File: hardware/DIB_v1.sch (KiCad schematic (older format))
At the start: 2 parts, among them J1 20-pin power socket, J2 Conn_02x14_Odd_Even

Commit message: Adding Bias_PS from dcm220
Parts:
- added C? (x4): 100n, EEZ DIB DCM220 r2B7:C0603, symbol EEZ_DIB_DCM220_r2B7-eagle-import:C-EUC0603
- added IC?: Si8662AB-B-IS1, EEZ DIB DCM220 r2B7:SOIC-16, symbol EEZ_DIB_DCM220_r2B7-eagle-import:SI8662NSOIC-16
- added IC?: Si8641AB-B-IS1, EEZ DIB DCM220 r2B7:SOIC-16, symbol EEZ_DIB_DCM220_r2B7-eagle-import:SI8641NSOIC-16
- added RN? (x4): DR1206-33R-4/8, EEZ DIB DCM220 r2B7:CAY16, symbol EEZ_DIB_DCM220_r2B7-eagle-import:R_ARRAY4
- added TX_PU?: 10K, EEZ DIB DCM220 r2B7:R0805, symbol EEZ_DIB_DCM220_r2B7-eagle-import:R-EU_R0805
- added X? (x24): 77317-104-28LF, EEZ DIB DCM220 r2B7:77317-104-28LF, symbol EEZ_DIB_DCM220_r2B7-eagle-import:77317-104-28LF
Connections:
- net labels added: +3V3, +VAUX, BOOT0, DIB_A0, DIB_A1, DIB_A2, DIB_BOOT0, DIB_CSA, DIB_CSB, DIB_IRQ, DIB_MISO, DIB_MOSI, DIB_NFAULT, DIB_NRESET, DIB_SCL, DIB_SCLK, DIB_SDA, DIB_SYNC, DIB_UART_RX, DIB_UART_TX, GND, GNDIO, IRQ, MISO, MOSI, NSS, OE_SYNC, SCLK, UART_RX, UART_TX, V+, ~RESET
- wire segments 20 -> 111
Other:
- note added: "+12V 21"
- note added: "+3V3 1"
- note added: "+5V 23"
- note added: "10 DIB_IRQ"
- note added: "12 DIB_CSB"
- note added: "14 DIB_MISO"
- note added: "16 Gnd"
- note added: "18 DIB_A2"
- note added: "2 +Vaux"
- note added: "20 Gnd"
- note added: "22 +12V"
- note added: "24 +5V"
- note added: "26 BOOT"
- note added: "28 UART_TX"
- note added: "28-pin module socket"
- note added: "4 NRESET"
- note added: "6 OE_SYNC"
- note added: "8 DIB_SDA"
- note added: "Bus isolator"
- note added: "DIB v1.0 connector"
- note added: "DIB_A0 17"
- note added: "DIB_A1 19"
- note added: "DIB_CSA 9"
- note added: "DIB_MOSI 15"
- note added: "DIB_SCL 5"
- note added: "DIB_SCLK 13"
- note added: "Gnd 11"
- note added: "Gnd 25"
- note added: "Gnd 7"
- note added: "Max. transfer speed is 1MBit/s"
- note added: "NFAULT 3"
- note added: "UART_RX 27"

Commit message: Adding ULX3S connections
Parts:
- removed C? (x4): 100n, EEZ DIB DCM220 r2B7:C0603, symbol EEZ_DIB_DCM220_r2B7-eagle-import:C-EUC0603
- removed IC?: Si8662AB-B-IS1, EEZ DIB DCM220 r2B7:SOIC-16, symbol EEZ_DIB_DCM220_r2B7-eagle-import:SI8662NSOIC-16
- removed IC?: Si8641AB-B-IS1, EEZ DIB DCM220 r2B7:SOIC-16, symbol EEZ_DIB_DCM220_r2B7-eagle-import:SI8641NSOIC-16
- removed J2: Conn_02x14_Odd_Even, Connector_PinHeader_2.54mm:PinHeader_2x14_P2.54mm_Horizontal, symbol Connector_Generic:Conn_02x14_Odd_Even
- removed RN? (x4): DR1206-33R-4/8, EEZ DIB DCM220 r2B7:CAY16, symbol EEZ_DIB_DCM220_r2B7-eagle-import:R_ARRAY4
- removed TX_PU?: 10K, EEZ DIB DCM220 r2B7:R0805, symbol EEZ_DIB_DCM220_r2B7-eagle-import:R-EU_R0805
- removed X? (x24): 77317-104-28LF, EEZ DIB DCM220 r2B7:77317-104-28LF, symbol EEZ_DIB_DCM220_r2B7-eagle-import:77317-104-28LF
- added J3: 28-pin module socket, Connector_PinHeader_2.54mm:PinHeader_2x14_P2.54mm_Horizontal, symbol Connector_Generic:Conn_02x14_Odd_Even
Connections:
- net labels added: +12V, +5V, A0, A1, A2, BOOT, CSA, CSB, NFAULT, NRESET, SSCL, SSDA, SYNC
- net labels removed: BOOT0, DIB_A0, DIB_A1, DIB_A2, DIB_BOOT0, DIB_CSA, DIB_CSB, DIB_IRQ, DIB_MISO, DIB_MOSI, DIB_NFAULT, DIB_NRESET, DIB_SCL, DIB_SCLK, DIB_SDA, DIB_SYNC, DIB_UART_RX, DIB_UART_TX, GNDIO, NSS, OE_SYNC, V+, ~RESET
- wire segments 111 -> 48
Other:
- note removed: "28-pin module socket"
- note removed: "Bus isolator"
- note removed: "Max. transfer speed is 1MBit/s"

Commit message: Assigning footprints
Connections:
- net +5V renamed 5V
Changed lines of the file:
@@
 +12V
 Text GLabel 3600 2150 0    50   Input ~ 0
-+5V
+5V
 Text GLabel 3600 2250 0    50   Input ~ 0
 BOOT
@@
 +12V
 Text GLabel 4300 2150 2    50   Input ~ 0
-+5V
+5V
 Text GLabel 4300 2250 2    50   Input ~ 0
 GND

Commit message: Adding last known changes to shematics
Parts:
- added C?: 100n, Capacitor_SMD:C_0603_1608Metric, symbol LCD_PMOD-rescue:C-EUC0603-EEZ_DIB_DCM220_r2B7-eagle-import
- added IC?: M24C32-WMN6P, OPA2211:SOIC127P600X170-9N, symbol LCD_PMOD-rescue:AT24CXXSOIC8-EEZ_DIB_DCM220_r2B7-eagle-import
- added R? (x3): 10K, Capacitor_SMD:C_0805_2012Metric, symbol LCD_PMOD-rescue:R-EU_R0805-EEZ_DIB_DCM220_r2B7-eagle-import
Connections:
- net A0: now also IC?.1 (A0), R?.2
- net A1: now also IC?.2 (A1), R?.2
- net A2: now also IC?.3 (A2), R?.2
- net GND: now also C?.1, IC?.4 (GND), IC?.7 (WP)
- net SSCL: now also IC?.6 (SCL)
- net SSDA: now also IC?.5 (SDA)
- new net 3V3: C?.2, IC?.8 (VCC), R?.1, R?.1, R?.1
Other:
- note added: "I2C Module ID EEPROM"
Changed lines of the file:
@@
 $Descr A4 11693 8268
 encoding utf-8
-Sheet 4 11
+Sheet 4 10
 Title ""
-Date ""
-Rev ""
-Comp ""
+Date "2020-01-29"
+Rev "0.1"
+Comp "Envox d.o.o."
 Comment1 ""
 Comment2 ""
@@
 Wire Notes Line
 	6700 900  6700 2500
+Wire Wire Line
+	9400 1550 9700 1550
+Wire Wire Line
+	9700 1550 9700 2350
+Wire Wire Line
+	9700 2350 9700 2650
+Wire Wire Line
+	9700 2650 9400 2650
+Text Label 7800 2350 0    50   ~ 0
+DIB_A0
+Connection ~ 9700 2350
+Wire Wire Line
+	9400 1650 9600 1650
+Wire Wire Line
+	9600 1650 9600 2250
+Wire Wire Line
+	9600 2250 9600 2550
+Wire Wire Line
+	9600 2550 9400 2550
+Text Label 7800 2250 0    50   ~ 0
+DIB_A1
+Connection ~ 9600 2250
+Wire Wire Line
+	9400 1750 9500 1750
+Wire Wire Line
+	9500 1750 9500 2150
+Wire Wire Line
+	9500 2150 9500 2450
+Wire Wire Line
+	9500 2450 9400 2450
+Text Label 7800 2150 0    50   ~ 0
+DIB_A2
+Connection ~ 9500 2150
+Text Label 7800 1350 0    50   ~ 0
+DIB_SCL
+Text Label 7800 1450 0    50   ~ 0
+DIB_SDA
+Wire Wire Line
+	8400 1550 8300 1550
+Wire Wire Line
+	8300 1550 8300 1750
+Wire Wire Line
+	8300 1750 8400 1750
+Wire Wire Line
+	8300 1850 8300 1750
+Connection ~ 8300 1750
+Text Label 8400 1550 0    10   ~ 0
+GNDIO
+Wire Wire Line
+	9900 1350 10000 1350
+Text Label 9900 1350 0    10   ~ 0
+GNDIO
+Wire Wire Line
+	9400 1350 9500 1350
+Wire Wire Line
+	9600 1350 9500 1350
+Connection ~ 9500 1350
+Text Label 9400 1350 0    10   ~ 0
+V+
+Wire Wire Line
+	9000 2450 8800 2450
+Wire Wire Line
+	8800 2450 8800 2550
+Wire Wire Line
+	8800 2550 8800 2650
+Wire Wire Line
+	8800 2650 9000 2650
+Wire Wire Line
+	9000 2550 8800 2550
+Connection ~ 8800 2550
+Connection ~ 8800 2450
+Text Label 9000 2450 0    10   ~ 0
+V+
+$Comp
+L LCD_PMOD-rescue:C-EUC0603-EEZ_DIB_DCM220_r2B7-eagle-import C?
+U 1 0 5E650AE0
+P 9800 1350
+AR Path="/5E650AE0" Ref="C?"  Part="1"
+AR Path="/5E155363/5E650AE0" Ref="C?"  Part="1"
+AR Path="/5E500AA4/5E650AE0" Ref="C?"  Part="1"
+AR Path="/5E22C9F9/5E650AE0" Ref="C?"  Part="1"
+F 0 "C?" V 9785 1335 59  0000 L BNN
+F 1 "100n" V 9885 1335 59  0000 L BNN
+F 2 "Capacitor_SMD:C_0603_1608Metric" H 9800 1350 50  0001 C CNN
+F 3 "" H 9800 1350 50  0001 C CNN
+	1    9800 1350
+	0    1    1    0
+$EndComp
+$Comp
+L LCD_PMOD-rescue:R-EU_R0805-EEZ_DIB_DCM220_r2B7-eagle-import R?
+U 1 0 5E650AE7
+P 9200 2450
+AR Path="/5E650AE7" Ref="R?"  Part="1"
+AR Path="/5E155363/5E650AE7" Ref="R?"  Part="1"
+AR Path="/5E500AA4/5E650AE7" Ref="R?"  Part="1"
+AR Path="/5E22C9F9/5E650AE7" Ref="R?"  Part="1"
+F 0 "R?" H 9300 2359 59  0000 L BNN
+F 1 "10K" H 9075 2430 59  0000 R TNN
+F 2 "Capacitor_SMD:C_0805_2012Metric" H 9200 2450 50  0001 C CNN
+F 3 "" H 9200 2450 50  0001 C CNN
+	1    9200 2450
+	1    0    0    1
+$EndComp
+$Comp
+L LCD_PMOD-rescue:R-EU_R0805-EEZ_DIB_DCM220_r2B7-eagle-import R?
+U 1 0 5E650AEE
+P 9200 2550
+AR Path="/5E650AEE" Ref="R?"  Part="1"
+AR Path="/5E155363/5E650AEE" Ref="R?"  Part="1"
+AR Path="/5E500AA4/5E650AEE" Ref="R?"  Part="1"
+AR Path="/5E22C9F9/5E650AEE" Ref="R?"  Part="1"
+F 0 "R?" H 9300 2459 59  0000 L BNN
+F 1 "10K" H 9075 2530 59  0000 R TNN
+F 2 "Capacitor_SMD:C_0805_2012Metric" H 9200 2550 50  0001 C CNN
+F 3 "" H 9200 2550 50  0001 C CNN
+	1    9200 2550
+	1    0    0    1
+$EndComp
+$Comp
+L LCD_PMOD-rescue:R-EU_R0805-EEZ_DIB_DCM220_r2B7-eagle-import R?
+U 1 0 5E650AF5
+P 9200 2650
+AR Path="/5E650AF5" Ref="R?"  Part="1"
+AR Path="/5E155363/5E650AF5" Ref="R?"  Part="1"
+AR Path="/5E500AA4/5E650AF5" Ref="R?"  Part="1"
+AR Path="/5E22C9F9/5E650AF5" Ref="R?"  Part="1"
+F 0 "R?" H 9300 2559 59  0000 L BNN
+F 1 "10K" H 9075 2630 59  0000 R TNN
+F 2 "Capacitor_SMD:C_0805_2012Metric" H 9200 2650 50  0001 C CNN
+F 3 "" H 9200 2650 50  0001 C CNN
+	1    9200 2650
+	1    0    0    1
+$EndComp
+$Comp
+L LCD_PMOD-rescue:AT24CXXSOIC8-EEZ_DIB_DCM220_r2B7-eagle-import IC?
+U 1 0 5E650AFC
+P 8900 1550
+AR Path="/5E650AFC" Ref="IC?"  Part="1"
+AR Path="/5E155363/5E650AFC" Ref="IC?"  Part="1"
+AR Path="/5E500AA4/5E650AFC" Ref="IC?"  Part="1"
+AR Path="/5E22C9F9/5E650AFC" Ref="IC?"  Part="1"
+F 0 "IC?" H 8814 1884 69  0000 L BNN
+F 1 "M24C32-WMN6P" H 8464 1133 69  0000 L BNN
+F 2 "OPA2211:SOIC127P600X170-9N" H 8900 1550 50  0001 C CNN
+F 3 "" H 8900 1550 50  0001 C CNN
+	1    8900 1550
+	1    0    0    -1
+$EndComp
+Text Notes 7600 850  0    59   ~ 0
+I2C Module ID EEPROM
+Text GLabel 7700 1450 0    50   Input ~ 0
+SSDA
+Wire Wire Line
+	7700 1450 8400 1450
+Text GLabel 7700 1350 0    50   Input ~ 0
+SSCL
+Wire Wire Line
+	7700 1350 8400 1350
+Text GLabel 7700 2350 0    50   Input ~ 0
+A0
+Text GLabel 7700 2250 0    50   Input ~ 0
+A1
+Text GLabel 7700 2150 0    50   Input ~ 0
+A2
+Wire Wire Line
+	7700 2150 9500 2150
+Wire Wire Line
+	7700 2250 9600 2250
+Wire Wire Line
+	7700 2350 9700 2350
+Text GLabel 10000 1550 3    50   Input ~ 0
+GND
+Wire Wire Line
+	10000 1350 10000 1550
+Text GLabel 8300 1850 3    50   Input ~ 0
+GND
+Text GLabel 9500 1150 1    50   Input ~ 0
+3V3
+Text GLabel 8600 2450 0    50   Input ~ 0
+3V3
+Wire Wire Line
+	9500 1150 9500 1350
+Wire Wire Line
+	8600 2450 8800 2450
 $EndSCHEMATC

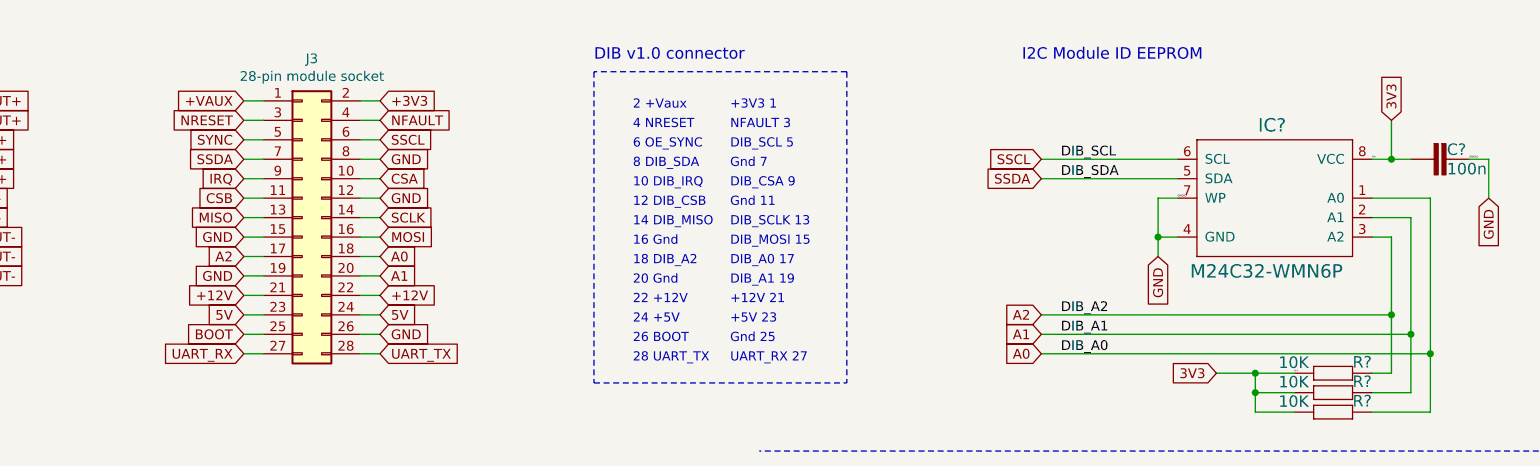
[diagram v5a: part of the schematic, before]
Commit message: Renaming wires
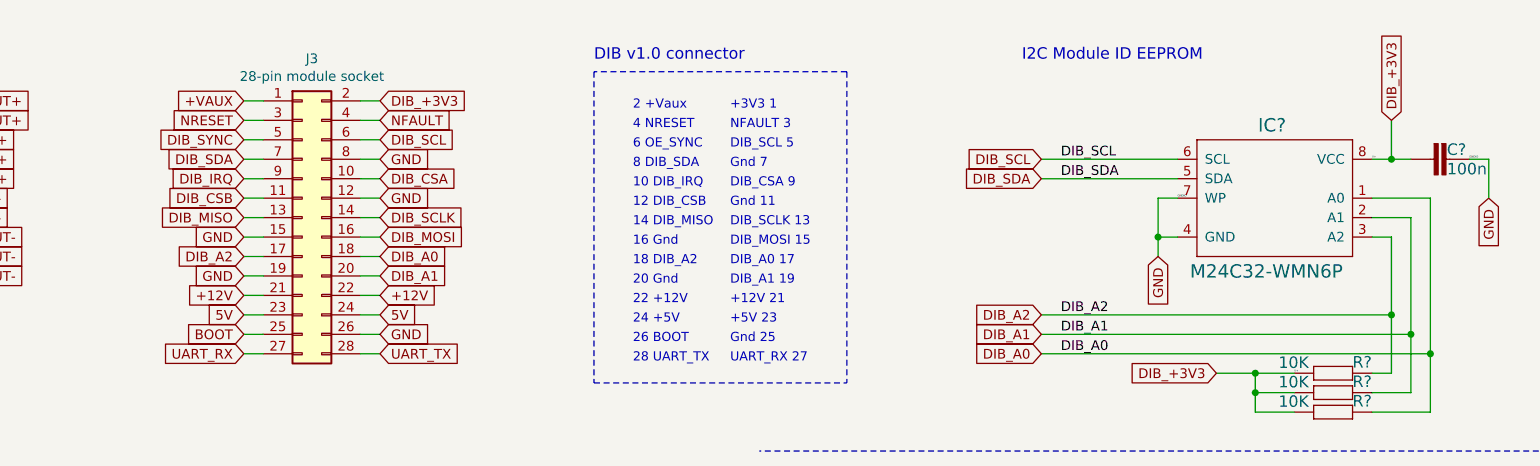
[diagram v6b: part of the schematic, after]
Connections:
- net 3V3 is gone; now on net DIB_+3V3: C?.2, IC?.8 (VCC), R?.1, R?.1, R?.1
- net +3V3 renamed DIB_+3V3
- net A0 renamed DIB_A0
- net A1 renamed DIB_A1
- net A2 renamed DIB_A2
- net CSA renamed DIB_CSA
- net CSB renamed DIB_CSB
- net IRQ renamed DIB_IRQ
- net MISO renamed DIB_MISO
- net MOSI renamed DIB_MOSI
- net SCLK renamed DIB_SCLK
- net SSCL renamed DIB_SCL
- net SSDA renamed DIB_SDA
- net SYNC renamed DIB_SYNC
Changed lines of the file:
@@
 NRESET
 Text GLabel 3600 1250 0    50   Input ~ 0
-SYNC
+DIB_SYNC
 Text GLabel 3600 1350 0    50   Input ~ 0
-SSDA
+DIB_SDA
 Text GLabel 3600 1450 0    50   Input ~ 0
-IRQ
+DIB_IRQ
 Text GLabel 3600 1550 0    50   Input ~ 0
-CSB
+DIB_CSB
 Text GLabel 3600 1650 0    50   Input ~ 0
-MISO
+DIB_MISO
 Text GLabel 3600 1750 0    50   Input ~ 0
 GND
 Text GLabel 3600 1850 0    50   Input ~ 0
-A2
+DIB_A2
 Text GLabel 3600 1950 0    50   Input ~ 0
 GND
@@
 UART_RX
 Text GLabel 4300 1050 2    50   Input ~ 0
-+3V3
+DIB_+3V3
 Text GLabel 4300 1150 2    50   Input ~ 0
 NFAULT
 Text GLabel 4300 1250 2    50   Input ~ 0
-SSCL
+DIB_SCL
 Text GLabel 4300 1350 2    50   Input ~ 0
 GND
@@
 GND
 Text GLabel 4300 1450 2    50   Input ~ 0
-CSA
+DIB_CSA
 Text GLabel 4300 1650 2    50   Input ~ 0
-SCLK
+DIB_SCLK
 Text GLabel 4300 1750 2    50   Input ~ 0
-MOSI
+DIB_MOSI
 Text GLabel 4300 1850 2    50   Input ~ 0
-A0
+DIB_A0
 Text GLabel 4300 1950 2    50   Input ~ 0
-A1
+DIB_A1
 Text GLabel 4300 2050 2    50   Input ~ 0
 +12V
@@
 I2C Module ID EEPROM
 Text GLabel 7700 1450 0    50   Input ~ 0
-SSDA
+DIB_SDA
 Wire Wire Line
 	7700 1450 8400 1450
 Text GLabel 7700 1350 0    50   Input ~ 0
-SSCL
+DIB_SCL
 Wire Wire Line
 	7700 1350 8400 1350
 Text GLabel 7700 2350 0    50   Input ~ 0
-A0
+DIB_A0
 Text GLabel 7700 2250 0    50   Input ~ 0
-A1
+DIB_A1
 Text GLabel 7700 2150 0    50   Input ~ 0
-A2
+DIB_A2
 Wire Wire Line
 	7700 2150 9500 2150
@@
 Text GLabel 8300 1850 3    50   Input ~ 0
 GND
+Text GLabel 8600 2450 0    50   Input ~ 0
+DIB_+3V3
+Wire Wire Line
+	9500 1150 9500 1350
+Wire Wire Line
+	8600 2450 8800 2450
 Text GLabel 9500 1150 1    50   Input ~ 0
-3V3
-Text GLabel 8600 2450 0    50   Input ~ 0
-3V3
-Wire Wire Line
-	9500 1150 9500 1350
-Wire Wire Line
-	8600 2450 8800 2450
+DIB_+3V3
 $EndSCHEMATC

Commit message: Routing board
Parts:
- added J17: FTDI, Connector_PinHeader_2.54mm:PinHeader_2x03_P2.54mm_Vertical, symbol Connector_Generic:Conn_02x03_Odd_Even
- gave numbers to parts that had none: 5
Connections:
- net GND: now also J17.2 (Pin_2)
- new net 3V3: J17.1 (Pin_1)
- new net TCK: J17.3 (Pin_3)
- new net TDI: J17.4 (Pin_4)
- new net TDO: J17.5 (Pin_5)
- new net TMS: J17.6 (Pin_6)
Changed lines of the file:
@@
 AR Path="/5E155363/5E650AE0" Ref="C?"  Part="1"
 AR Path="/5E500AA4/5E650AE0" Ref="C?"  Part="1"
-AR Path="/5E22C9F9/5E650AE0" Ref="C?"  Part="1"
-F 0 "C?" V 9785 1335 59  0000 L BNN
+AR Path="/5E22C9F9/5E650AE0" Ref="C25"  Part="1"
+F 0 "C25" V 9785 1335 59  0000 L BNN
 F 1 "100n" V 9885 1335 59  0000 L BNN
 F 2 "Capacitor_SMD:C_0603_1608Metric" H 9800 1350 50  0001 C CNN
@@
 AR Path="/5E155363/5E650AE7" Ref="R?"  Part="1"
 AR Path="/5E500AA4/5E650AE7" Ref="R?"  Part="1"
-AR Path="/5E22C9F9/5E650AE7" Ref="R?"  Part="1"
-F 0 "R?" H 9300 2359 59  0000 L BNN
+AR Path="/5E22C9F9/5E650AE7" Ref="R13"  Part="1"
+F 0 "R13" H 9300 2359 59  0000 L BNN
 F 1 "10K" H 9075 2430 59  0000 R TNN
 F 2 "Capacitor_SMD:C_0805_2012Metric" H 9200 2450 50  0001 C CNN
@@
 AR Path="/5E155363/5E650AEE" Ref="R?"  Part="1"
 AR Path="/5E500AA4/5E650AEE" Ref="R?"  Part="1"
-AR Path="/5E22C9F9/5E650AEE" Ref="R?"  Part="1"
-F 0 "R?" H 9300 2459 59  0000 L BNN
+AR Path="/5E22C9F9/5E650AEE" Ref="R14"  Part="1"
+F 0 "R14" H 9300 2459 59  0000 L BNN
 F 1 "10K" H 9075 2530 59  0000 R TNN
 F 2 "Capacitor_SMD:C_0805_2012Metric" H 9200 2550 50  0001 C CNN
@@
 AR Path="/5E155363/5E650AF5" Ref="R?"  Part="1"
 AR Path="/5E500AA4/5E650AF5" Ref="R?"  Part="1"
-AR Path="/5E22C9F9/5E650AF5" Ref="R?"  Part="1"
-F 0 "R?" H 9300 2559 59  0000 L BNN
+AR Path="/5E22C9F9/5E650AF5" Ref="R15"  Part="1"
+F 0 "R15" H 9300 2559 59  0000 L BNN
 F 1 "10K" H 9075 2630 59  0000 R TNN
 F 2 "Capacitor_SMD:C_0805_2012Metric" H 9200 2650 50  0001 C CNN
@@
 AR Path="/5E155363/5E650AFC" Ref="IC?"  Part="1"
 AR Path="/5E500AA4/5E650AFC" Ref="IC?"  Part="1"
-AR Path="/5E22C9F9/5E650AFC" Ref="IC?"  Part="1"
-F 0 "IC?" H 8814 1884 69  0000 L BNN
+AR Path="/5E22C9F9/5E650AFC" Ref="IC4"  Part="1"
+F 0 "IC4" H 8814 1884 69  0000 L BNN
 F 1 "M24C32-WMN6P" H 8464 1133 69  0000 L BNN
 F 2 "OPA2211:SOIC127P600X170-9N" H 8900 1550 50  0001 C CNN
@@
 Text GLabel 9500 1150 1    50   Input ~ 0
 DIB_+3V3
+$Comp
+L Connector_Generic:Conn_02x03_Odd_Even J?
+U 1 1 5E3DE14E
+P 3900 3100
+AR Path="/5E22C01C/5E3DE14E" Ref="J?"  Part="1"
+AR Path="/5E22C9F9/5E3DE14E" Ref="J17"  Part="1"
+F 0 "J17" H 3950 3417 50  0000 C CNN
+F 1 "FTDI" H 3950 3326 50  0000 C CNN
+F 2 "Connector_PinHeader_2.54mm:PinHeader_2x03_P2.54mm_Vertical" H 3900 3100 50  0001 C CNN
+F 3 "~" H 3900 3100 50  0001 C CNN
+	1    3900 3100
+	1    0    0    -1
+$EndComp
+Text GLabel 3600 3000 0    50   Input ~ 0
+3V3
+Text GLabel 3600 3100 0    50   Input ~ 0
+TCK
+Text GLabel 3600 3200 0    50   Input ~ 0
+TDO
+Text GLabel 4300 3000 2    50   Input ~ 0
+GND
+Text GLabel 4300 3100 2    50   Input ~ 0
+TDI
+Text GLabel 4300 3200 2    50   Input ~ 0
+TMS
+Wire Wire Line
+	3600 3000 3700 3000
+Wire Wire Line
+	3600 3100 3700 3100
+Wire Wire Line
+	3600 3200 3700 3200
+Wire Wire Line
+	4200 3000 4300 3000
+Wire Wire Line
+	4200 3100 4300 3100
+Wire Wire Line
+	4200 3200 4300 3200
 $EndSCHEMATC
